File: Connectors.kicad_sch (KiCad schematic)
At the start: 4 parts, among them J1 Conn_01x04_Pin, J2 Conn_01x04_Pin, J3 Conn_01x09_Pin, J4 Conn_02x03_Odd_Even

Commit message: Associated all footprints to the symbols
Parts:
- J1, J2: footprint (none) -> Connector_PinHeader_2.54mm:PinHeader_1x04_P2.54mm_Vertical
- J3: footprint (none) -> Connector_PinHeader_2.54mm:PinHeader_1x09_P2.54mm_Vertical
- J4: footprint (none) -> Connector_PinHeader_2.54mm:PinHeader_2x03_P2.54mm_Vertical
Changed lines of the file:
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@@
 			)
 		)
-		(property "Footprint" ""
+		(property "Footprint" "Connector_PinHeader_2.54mm:PinHeader_1x04_P2.54mm_Vertical"
 			(at 198.12 76.2 0)
 			(effects
@@
 			)
 		)
-		(property "Footprint" ""
+		(property "Footprint" "Connector_PinHeader_2.54mm:PinHeader_2x03_P2.54mm_Vertical"
 			(at 234.95 76.2 0)
 			(effects
@@
 			)
 		)
-		(property "Footprint" ""
+		(property "Footprint" "Connector_PinHeader_2.54mm:PinHeader_1x04_P2.54mm_Vertical"
 			(at 214.63 76.2 0)
 			(effects
@@
 			)
 		)
-		(property "Footprint" ""
+		(property "Footprint" "Connector_PinHeader_2.54mm:PinHeader_1x09_P2.54mm_Vertical"
 			(at 182.88 81.28 0)
 			(effects

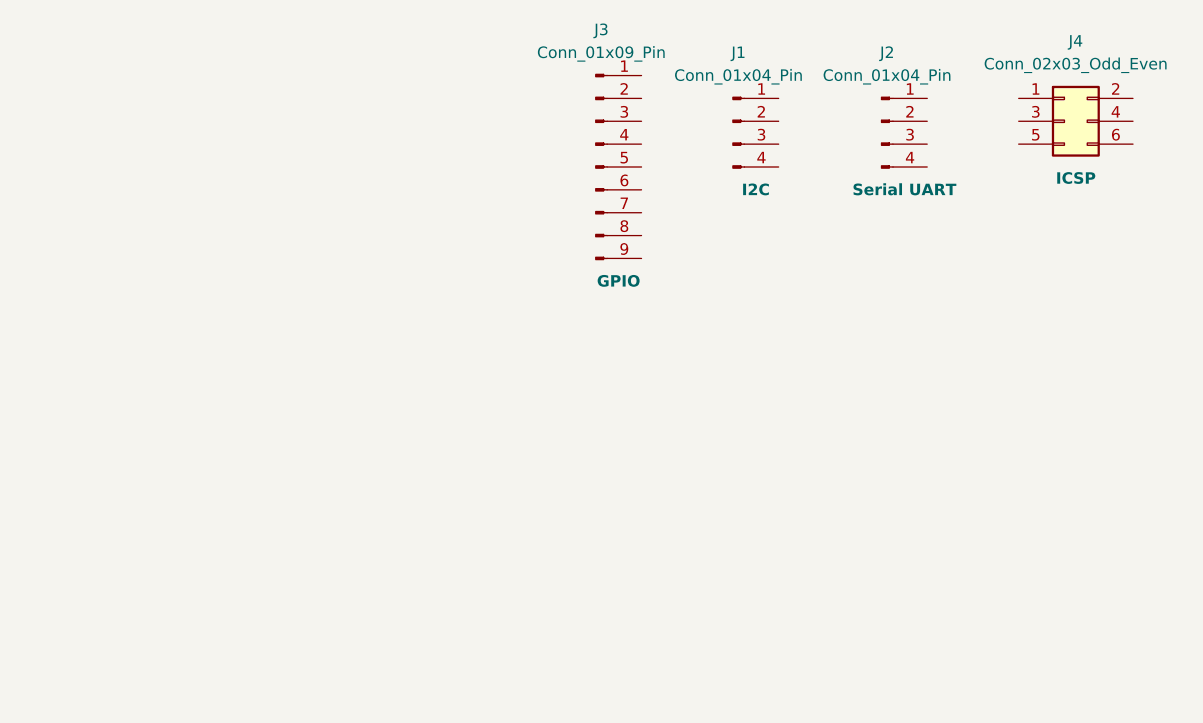
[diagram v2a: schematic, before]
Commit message: Net classes is added
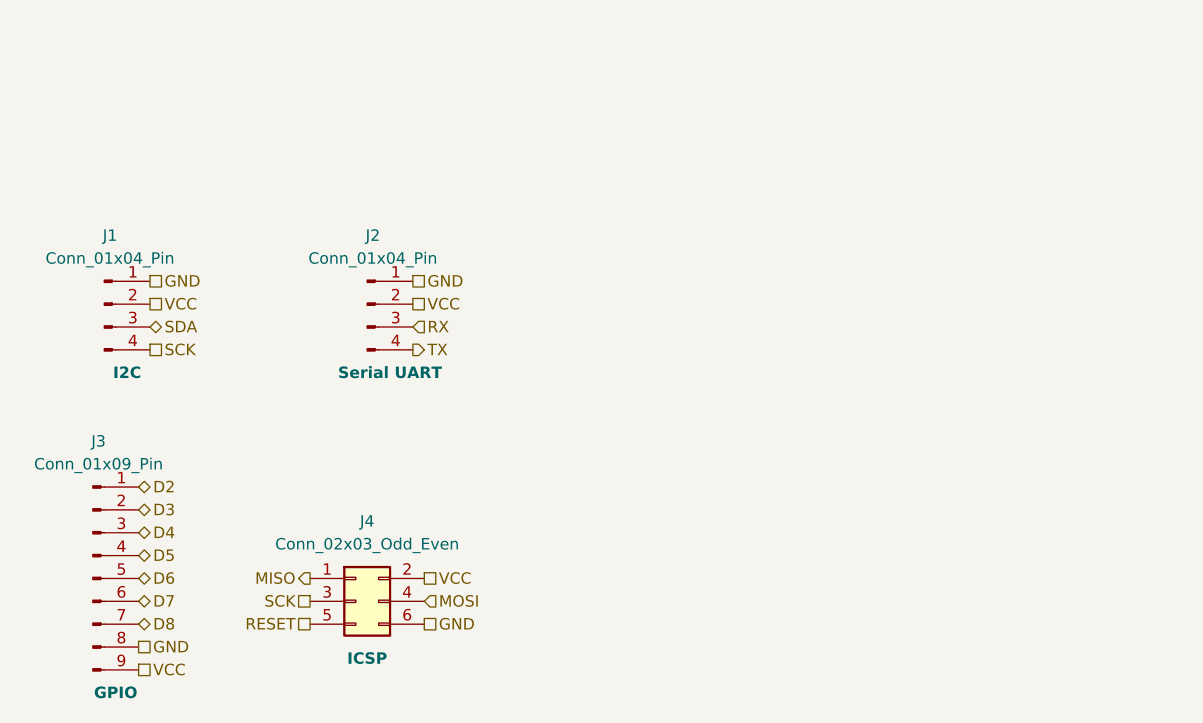
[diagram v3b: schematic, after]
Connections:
- net GND: now reaches J1.1 (Pin_1)
- net GND: now also J2.1 (Pin_1), J3.8 (Pin_8), J4.6 (Pin_6)
- net VCC: now reaches J1.2 (Pin_2)
- net VCC: now also J2.2 (Pin_2), J3.9 (Pin_9), J4.2 (Pin_2)
- net SDA: now reaches J1.3 (Pin_3)
- net SCK: now reaches J1.4 (Pin_4)
- net SCK: now also J4.3 (Pin_3)
- net MISO: now reaches J4.1 (Pin_1)
- net MOSI: now reaches J4.4 (Pin_4)
- net RESET: now reaches J4.5 (Pin_5)
- net RX: now reaches J2.3 (Pin_3)
- net TX: now reaches J2.4 (Pin_4)
- net D2: now reaches J3.1 (Pin_1)
- net D3: now reaches J3.2 (Pin_2)
- net D4: now reaches J3.3 (Pin_3)
- net D5: now reaches J3.4 (Pin_4)
- net D6: now reaches J3.5 (Pin_5)
- net D7: now reaches J3.6 (Pin_6)
- net D8: now reaches J3.7 (Pin_7)
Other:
- moved on the sheet: J1, J2, J3, J4

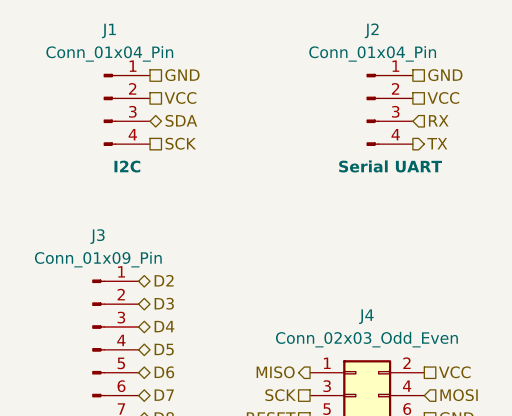
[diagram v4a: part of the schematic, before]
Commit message: Added & arranged footprints
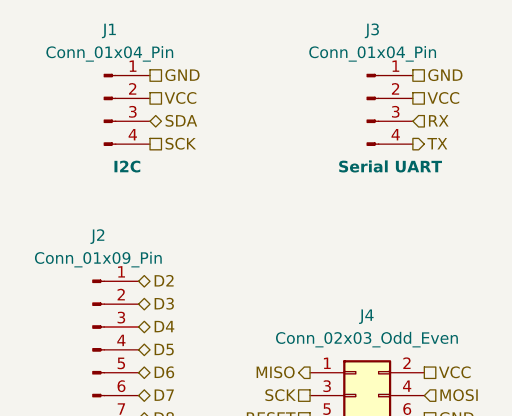
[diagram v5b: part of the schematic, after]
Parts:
- renumbered J3 to J2, J2 to J3
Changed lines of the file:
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@@
 		(on_board yes)
 		(dnp no)
-		(property "Reference" "J2"
+		(property "Reference" "J3"
 			(at 158.115 88.9 0)
 			(effects
@@
 			(project "MCU_DATALOGGER"
 				(path "/5f39d14e-0ef9-452b-b6b7-4a46ee7d59d6/4c157763-d996-4f97-b708-240f3d50c52b"
-					(reference "J2")
+					(reference "J3")
 					(unit 1)
 				)
@@
 		(on_board yes)
 		(dnp no)
-		(property "Reference" "J3"
+		(property "Reference" "J2"
 			(at 127.635 111.76 0)
 			(effects
@@
 			(project ""
 				(path "/5f39d14e-0ef9-452b-b6b7-4a46ee7d59d6/4c157763-d996-4f97-b708-240f3d50c52b"
-					(reference "J3")
+					(reference "J2")
 					(unit 1)
 				)
